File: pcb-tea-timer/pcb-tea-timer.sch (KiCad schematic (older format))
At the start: 7 parts, among them J1 Conn_01x07_Female, Q1 2N7002, SW1 SW_Push_Dual, SW2 SW_Push_Dual

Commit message: Tea timer PCB finished.
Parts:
- added C1, C2: 1nF, Capacitor_SMD:C_0805_2012Metric_Pad1.15x1.40mm_HandSolder, symbol Device:C
- added J2: Conn_01x02_Female, Connector_PinHeader_2.54mm:PinHeader_1x02_P2.54mm_Vertical, symbol Connector:Conn_01x02_Female
- BZ1: footprint (none) -> SS_Connectors:Round Piezo 1
- SW1, SW2: footprint (none) -> SS_Connectors:Push Button 12x12mm
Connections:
- net +5V: no longer R1.1
- net GND: now also R1.2, C1.2, C2.2, J2.1 (Pin_1), J2.2 (Pin_2)
- net at A1.11 (D8): now also J1.6 (Pin_6); no longer J1.5 (Pin_5)
- net at A1.12 (D9): now also J1.5 (Pin_5); no longer J1.6 (Pin_6)
- net at A1.5 (D2), SW1.1, SW1.3: now also C1.1
- net at A1.6 (D3), SW2.1, SW2.3: now also C2.1
- net at A1.9 (D6): now also Q1.1 (G), R1.1
- now unconnected: A1.10 (D7)
- no-connect marks 0 -> 18
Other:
- note added: "Physical support for the display"
- moved on the sheet: BZ1, J1, Q1, R1, SW1, SW2

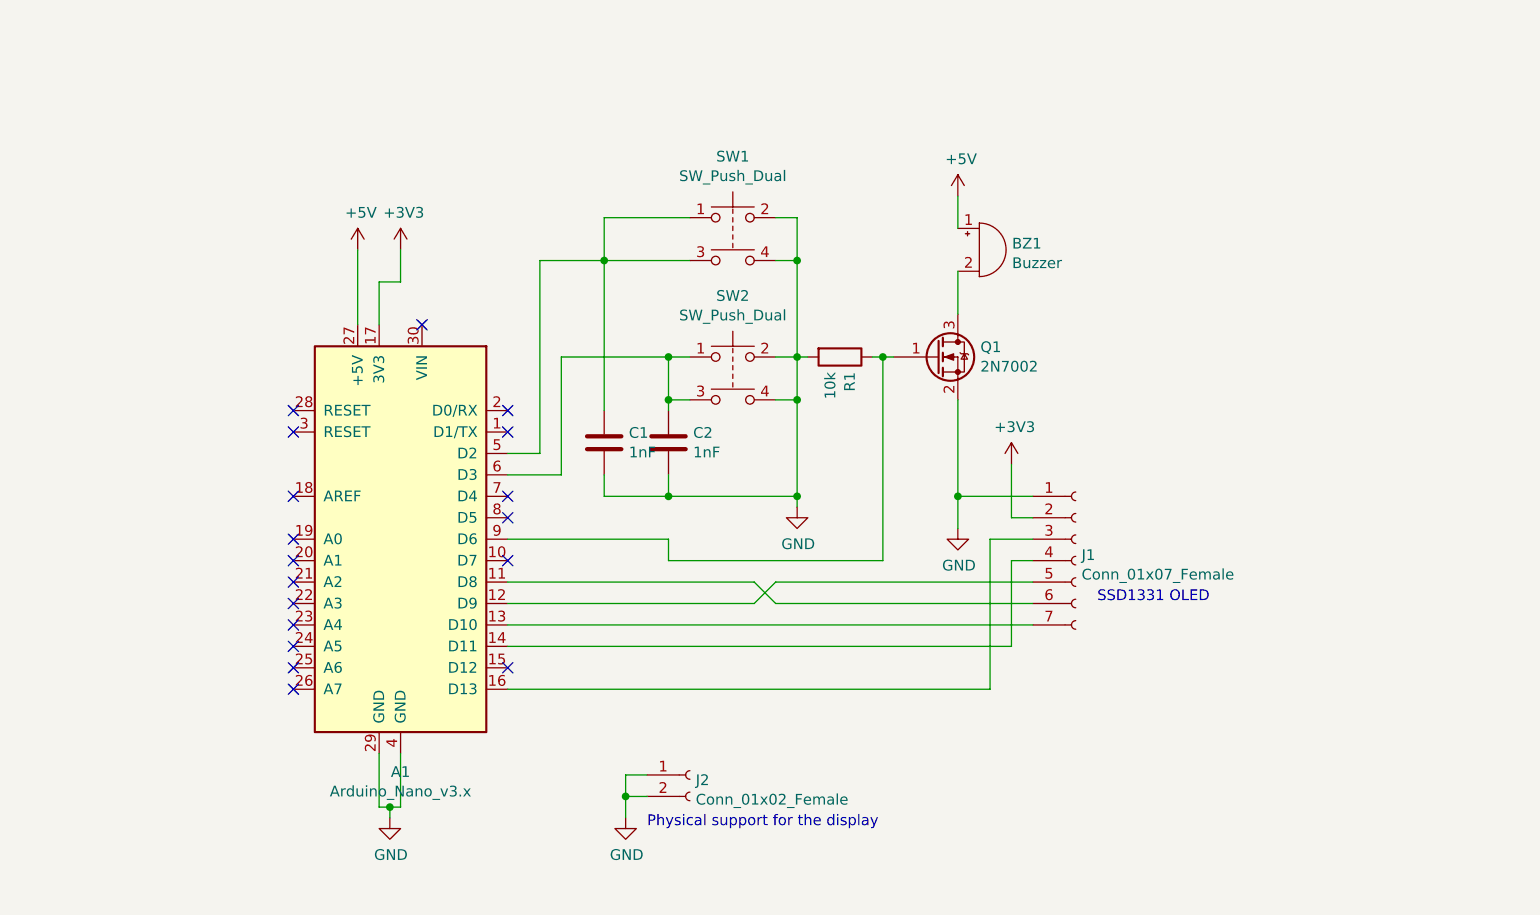
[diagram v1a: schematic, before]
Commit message: Pcb-tea-timer: fix piezo buzzer driving with a mosfet.
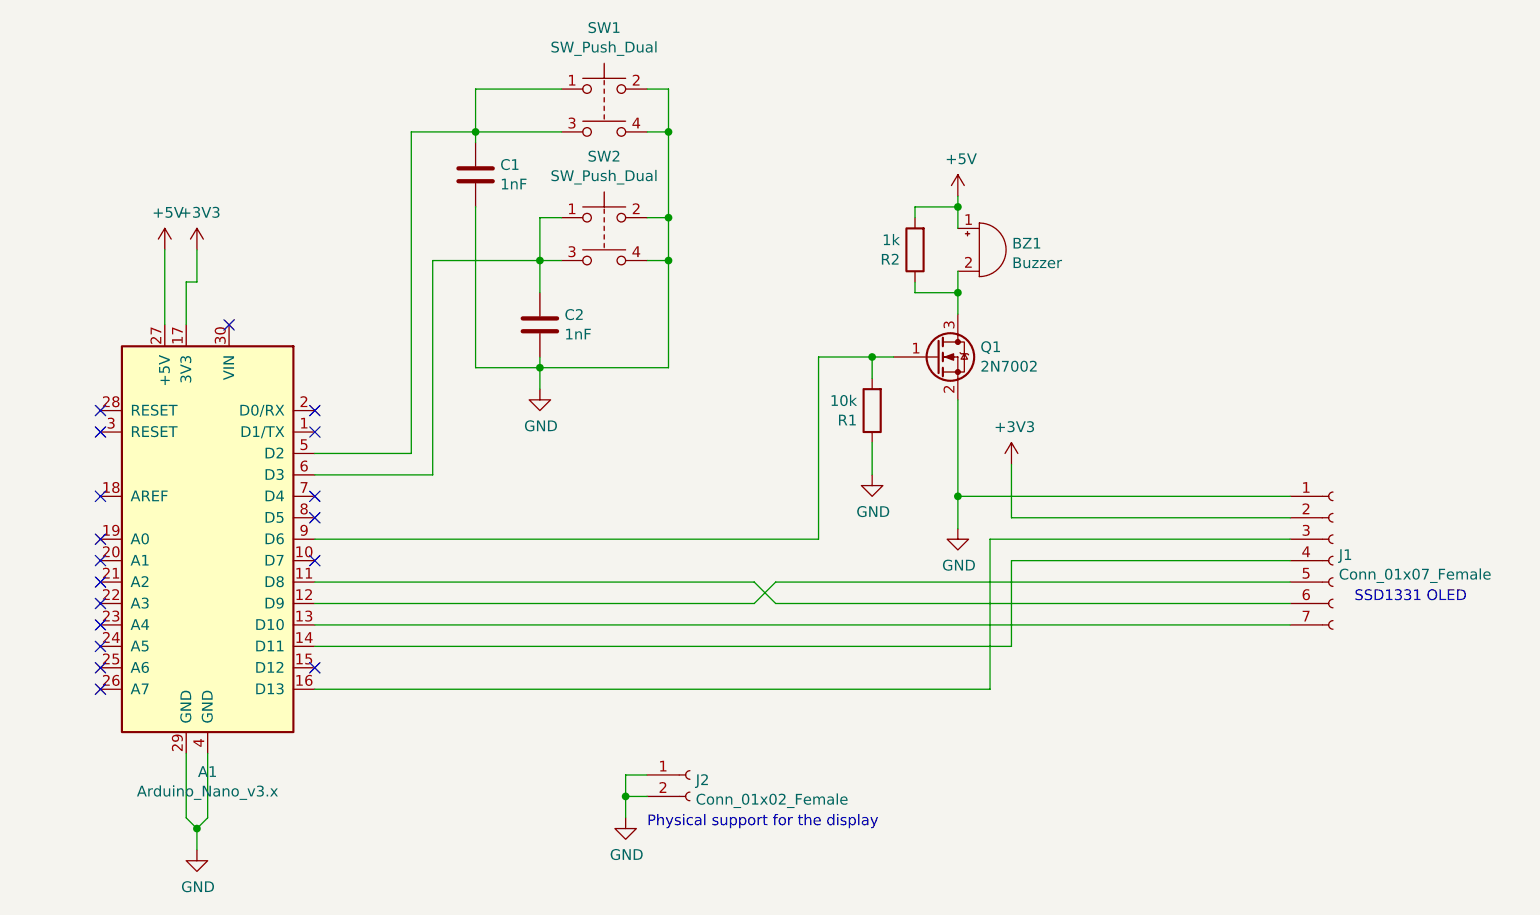
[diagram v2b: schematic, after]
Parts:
- added R2: 1k, Resistor_SMD:R_0805_2012Metric_Pad1.15x1.40mm_HandSolder, symbol Device:R
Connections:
- net +5V: now also R2.2
- net GND: now also R1.1; no longer R1.2
- net at A1.9 (D6), Q1.1 (G): now also R1.2; no longer R1.1
- net at BZ1.2 (+), Q1.3 (D): now also R2.1
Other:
- moved on the sheet: A1, C2, J1, R1, SW1, SW2

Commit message: Pcb-tea-timer: add capacitor to support vcc against drops
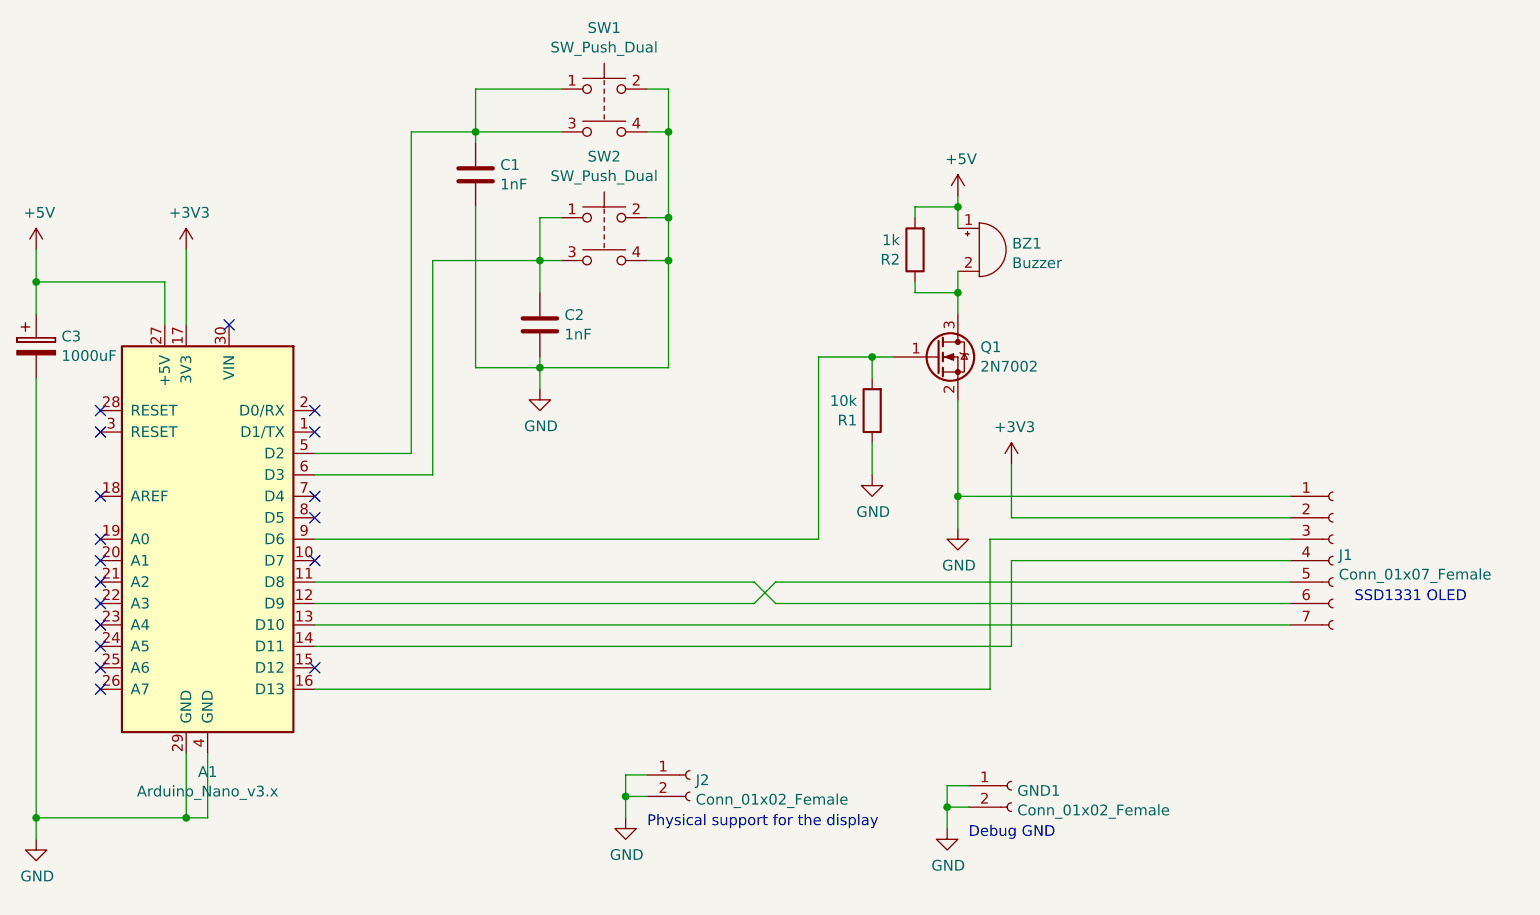
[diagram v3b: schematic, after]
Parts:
- added C3: 1000uF, Capacitor_THT:CP_Radial_D7.5mm_P2.50mm, symbol Device:CP
- added GND1: Conn_01x02_Female, Connector_PinHeader_2.54mm:PinHeader_1x02_P2.54mm_Vertical, symbol Connector:Conn_01x02_Female
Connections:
- net +5V: now also C3.1
- net GND: now also C3.2, GND1.1 (Pin_1), GND1.2 (Pin_2)
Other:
- note added: "Debug GND"
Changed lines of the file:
@@
 L power:+3V3 #PWR0102
 U 1 1 5C6E50A5
-P 3950 2800
-F 0 "#PWR0102" H 3950 2650 50  0001 C CNN
-F 1 "+3V3" H 3965 2973 50  0000 C CNN
-F 2 "" H 3950 2800 50  0001 C CNN
-F 3 "" H 3950 2800 50  0001 C CNN
-	1    3950 2800
+P 3900 2800
+F 0 "#PWR0102" H 3900 2650 50  0001 C CNN
+F 1 "+3V3" H 3915 2973 50  0000 C CNN
+F 2 "" H 3900 2800 50  0001 C CNN
+F 3 "" H 3900 2800 50  0001 C CNN
+	1    3900 2800
 	1    0    0    -1
 $EndComp
@@
 L power:+5V #PWR0103
 U 1 1 5C6E50D2
-P 3800 2800
-F 0 "#PWR0103" H 3800 2650 50  0001 C CNN
-F 1 "+5V" H 3815 2973 50  0000 C CNN
-F 2 "" H 3800 2800 50  0001 C CNN
-F 3 "" H 3800 2800 50  0001 C CNN
-	1    3800 2800
+P 3200 2800
+F 0 "#PWR0103" H 3200 2650 50  0001 C CNN
+F 1 "+5V" H 3215 2973 50  0000 C CNN
+F 2 "" H 3200 2800 50  0001 C CNN
+F 3 "" H 3200 2800 50  0001 C CNN
+	1    3200 2800
 	1    0    0    -1
 $EndComp
@@
 	7650 4850 4500 4850
 Wire Wire Line
-	3800 3150 3800 2800
+	3800 3150 3800 2950
 $Comp
 L power:GND #PWR0104
 U 1 1 5C6E6194
-P 3950 5600
-F 0 "#PWR0104" H 3950 5350 50  0001 C CNN
-F 1 "GND" H 3955 5427 50  0000 C CNN
-F 2 "" H 3950 5600 50  0001 C CNN
-F 3 "" H 3950 5600 50  0001 C CNN
-	1    3950 5600
+P 3200 5550
+F 0 "#PWR0104" H 3200 5300 50  0001 C CNN
+F 1 "GND" H 3205 5377 50  0000 C CNN
+F 2 "" H 3200 5550 50  0001 C CNN
+F 3 "" H 3200 5550 50  0001 C CNN
+	1    3200 5550
 	1    0    0    -1
 $EndComp
@@
 SSD1331 OLED
 Wire Wire Line
-	3900 5450 3950 5500
-Wire Wire Line
-	3950 5500 3950 5600
-Wire Wire Line
-	3950 5500 4000 5450
-Wire Wire Line
 	4000 5450 4000 5150
-Connection ~ 3950 5500
 $Comp
 L Device:Buzzer BZ1
@@
 	6550 4450 4500 4450
 Wire Wire Line
-	3950 2800 3950 2950
-Wire Wire Line
-	3950 2950 3900 2950
-Wire Wire Line
-	3900 2950 3900 3150
-Wire Wire Line
 	5550 3350 5550 3450
 $Comp
@@
 Wire Wire Line
 	5050 3850 4500 3850
+$Comp
+L Device:CP C3
+U 1 1 5D84E84F
+P 3200 3250
+F 0 "C3" H 3318 3296 50  0000 L CNN
+F 1 "1000uF" H 3318 3205 50  0000 L CNN
+F 2 "Capacitor_THT:CP_Radial_D7.5mm_P2.50mm" H 3238 3100 50  0001 C CNN
+F 3 "~" H 3200 3250 50  0001 C CNN
+	1    3200 3250
+	1    0    0    -1
+$EndComp
+Wire Wire Line
+	3200 3400 3200 5450
+Wire Wire Line
+	4000 5450 3900 5450
+Wire Wire Line
+	3900 5450 3200 5450
+Connection ~ 3900 5450
+Connection ~ 3200 5450
+Wire Wire Line
+	3200 5450 3200 5550
+Wire Wire Line
+	3200 3100 3200 2950
+Wire Wire Line
+	3200 2950 3800 2950
+Wire Wire Line
+	3200 2800 3200 2950
+Connection ~ 3200 2950
+Wire Wire Line
+	3900 2800 3900 3150
+$Comp
+L Connector:Conn_01x02_Female GND1
+U 1 1 5D857D76
+P 7750 5300
+F 0 "GND1" H 7777 5276 50  0000 L CNN
+F 1 "Conn_01x02_Female" H 7777 5185 50  0000 L CNN
+F 2 "Connector_PinHeader_2.54mm:PinHeader_1x02_P2.54mm_Vertical" H 7750 5300 50  0001 C CNN
+F 3 "~" H 7750 5300 50  0001 C CNN
+	1    7750 5300
+	1    0    0    -1
+$EndComp
+$Comp
+L power:GND #PWR0110
+U 1 1 5D857DB8
+P 7450 5500
+F 0 "#PWR0110" H 7450 5250 50  0001 C CNN
+F 1 "GND" H 7455 5327 50  0000 C CNN
+F 2 "" H 7450 5500 50  0001 C CNN
+F 3 "" H 7450 5500 50  0001 C CNN
+	1    7450 5500
+	1    0    0    -1
+$EndComp
+Wire Wire Line
+	7550 5300 7450 5300
+Wire Wire Line
+	7450 5300 7450 5400
+Wire Wire Line
+	7550 5400 7450 5400
+Connection ~ 7450 5400
+Wire Wire Line
+	7450 5400 7450 5500
+Text Notes 7550 5550 0    50   ~ 0
+Debug GND
 $EndSCHEMATC
